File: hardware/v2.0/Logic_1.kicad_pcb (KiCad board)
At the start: 2 copper layers, 100 x 100 mm, 83 parts, among them J1 Conn_02x06_Odd_Even, J10 Conn_01x04, J11 USB_C_Receptacle_USB2.0, J12 Conn_01x02, J13 Conn_01x03, J2 Micro_SD_Card, J3 Conn_01x06, J7 Conn_01x08, J8 USB_C_Receptacle_USB2.0, J9 Conn_01x04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

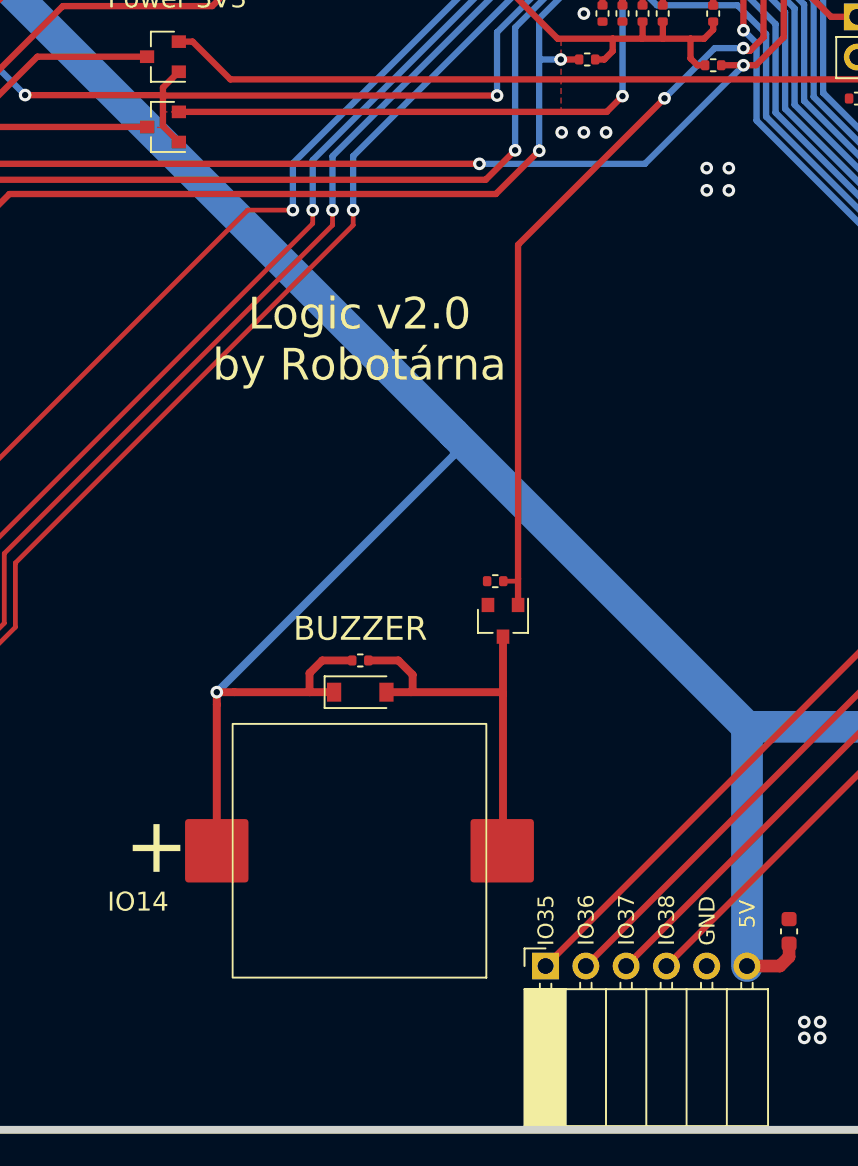
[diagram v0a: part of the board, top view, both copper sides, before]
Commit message: Change piezo
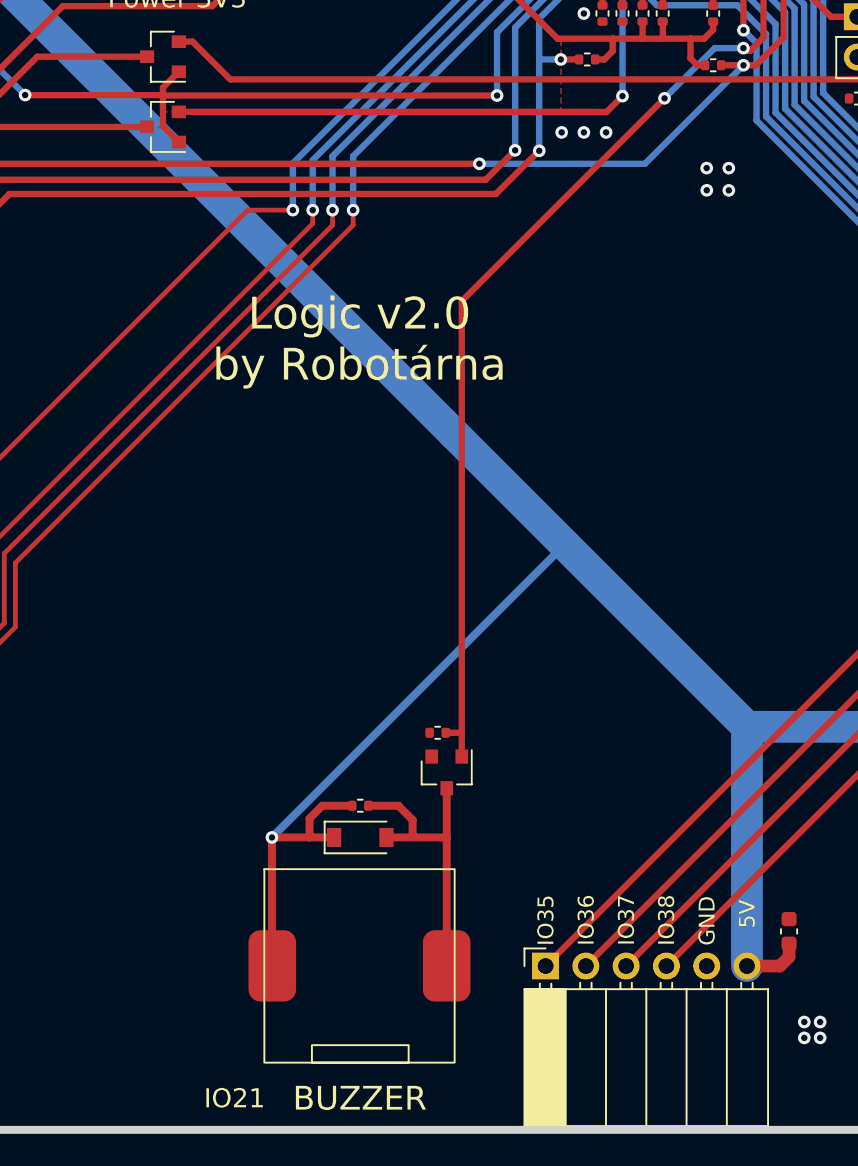
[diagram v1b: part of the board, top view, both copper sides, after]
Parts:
- BZ1: footprint Robotarna_KiCad_Library:ELKS-PIEZO -> Robotarna_KiCad_Library:PKLCS1212E-(RH-Logic_piezzo)
- moved R19 10.2 mm to (194.9, 120.0)
- moved Q6 10.2 mm to (195.4, 122.5)
- moved D114 9.16 mm to (190.0, 126.6)
- moved R33 9.16 mm to (190.0, 124.6)
- moved BZ1 7.26 mm to (189.9, 134.7), turned to 0 degrees
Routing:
- net /elektronika.sch/PIEZO: track 49.1 -> 60.1 mm
- net Net-(BZ1-Pad2): track 25.2 -> 19.2 mm
- net /elektronika.sch/5V: track 244.3 -> 242.5 mm
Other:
- board text added: "IO21"
- board text removed: "+"
- board text removed: "IO14"
